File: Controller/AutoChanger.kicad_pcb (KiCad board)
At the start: 2 copper layers, 118 x 74.1 mm, 32 parts, among them J1 OLED, P10 SENSOR, P11 SENSOR, P12 LOGO, P3 1, P4 2, P5 3, P6 4, P8 M3, P9 M3, SW1 RESET, SW2 1, SW3 2, SW4 3, SW5 4, SW6 PRGM, U1 TinyPico, U2 PCA9685PW, U3 ITR9606-F

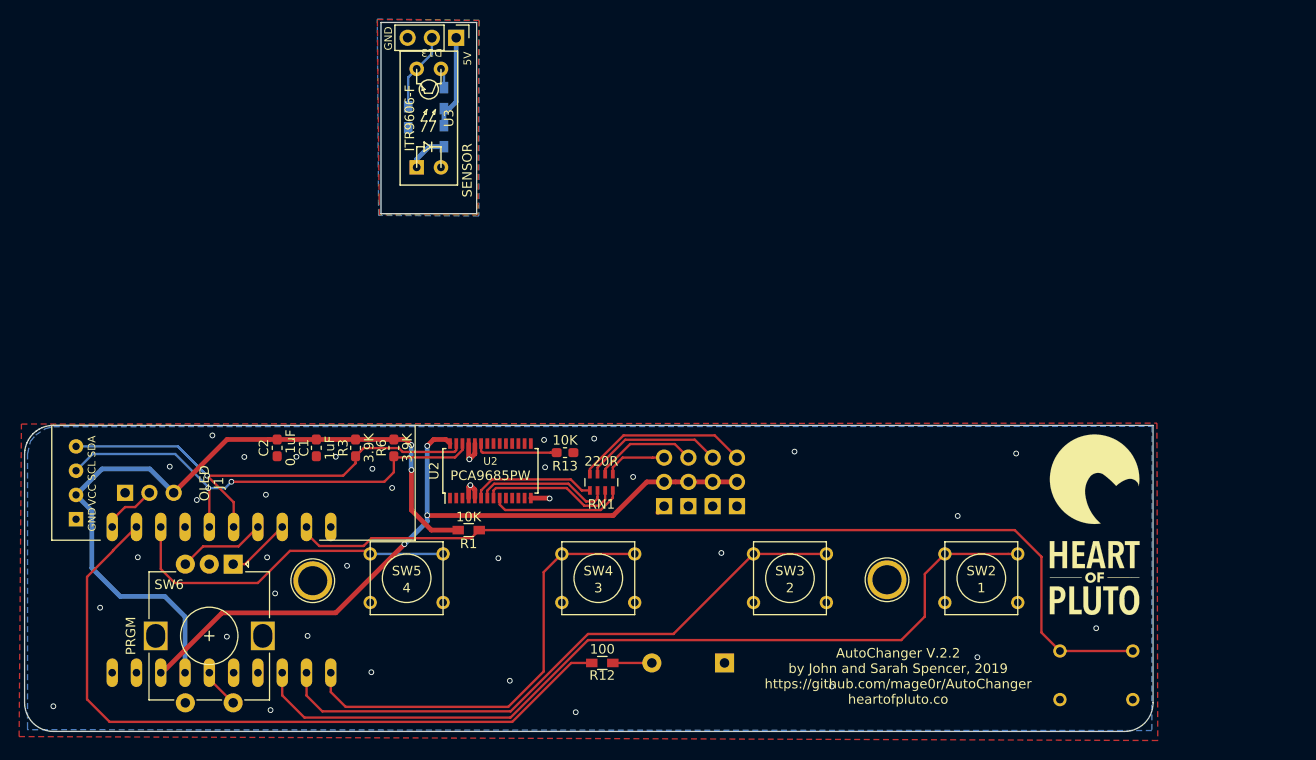
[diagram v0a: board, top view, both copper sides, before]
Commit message: Circuit Board updated to version 3.0
Circuit board no longer uses a TinyPICO.  It uses a ESP32-S3-WROOM module instead.  It is also 90% SMD parts and can be assembled by JLCPCB
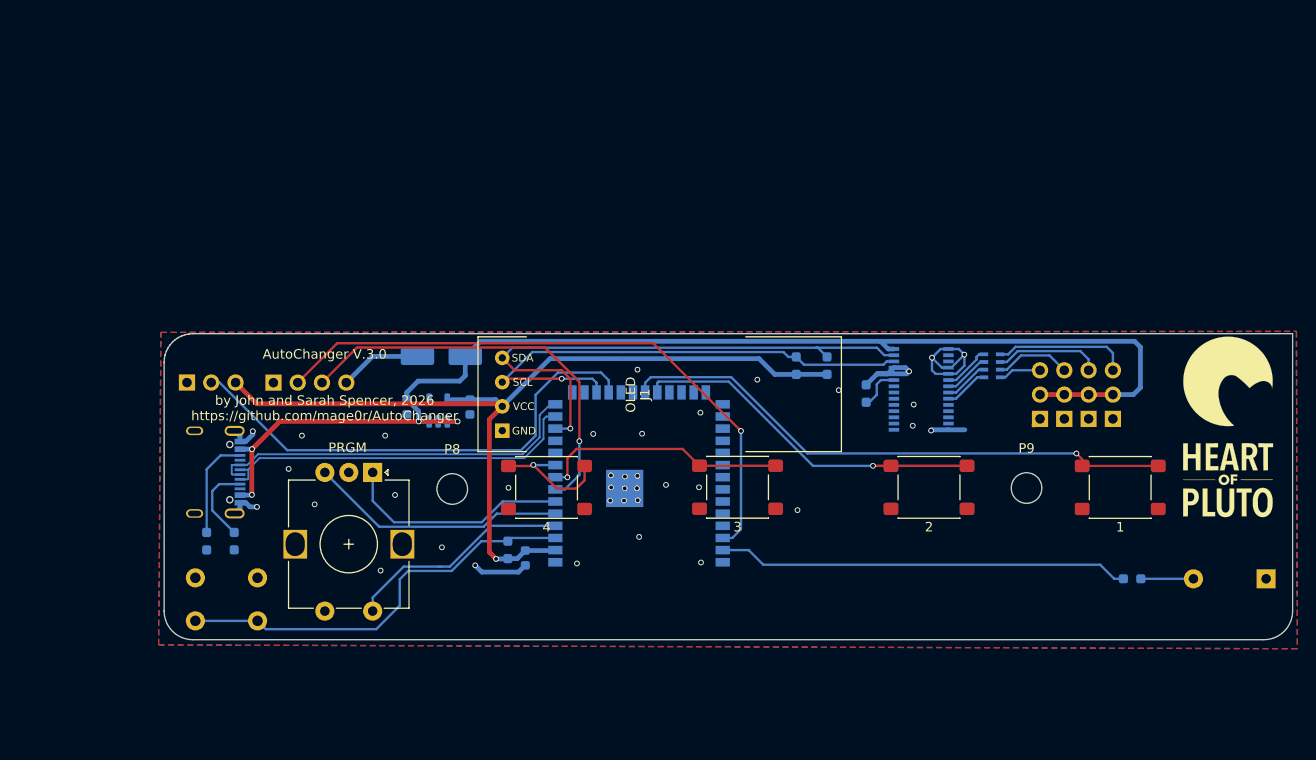
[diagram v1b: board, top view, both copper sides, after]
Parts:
- removed C1: 1uF, Capacitor_SMD:C_0603_1608Metric_Pad1.05x0.95mm_HandSolder
- removed C2: 0.1uF, Capacitor_SMD:C_0603_1608Metric_Pad1.05x0.95mm_HandSolder
- removed P11: SENSOR, Pin_Headers:Pin_Header_Straight_1x03_Pitch2.54mm
- removed R2, R4: 220R, Resistors_SMD:R_0603_HandSoldering
- removed R3, R6: 3.9K, Resistor_SMD:R_0603_1608Metric_Pad1.05x0.95mm_HandSolder
- removed R5: 2M, Resistors_SMD:R_0603_HandSoldering
- removed U1: TinyPico, libs:TinyPico
- removed U3: ITR9606-F, libs:ITR9606
- added C3: 22uF, Capacitor_SMD:C_0603_1608Metric, B.Cu at (141.6, 93.9)
- added C8: 10uF, Capacitor_SMD:C_0603_1608Metric, B.Cu at (129.2, 78.1)
- added C9: 10uF, Capacitor_SMD:C_0603_1608Metric, B.Cu at (135.8, 78.1)
- added D1: SS14, Diode_SMD:D_SMA_Handsoldering, B.Cu at (132.8, 72.8)
- added J2: USB-C, libs:AMPHENOL_12402012E212A, B.Cu at (107.0, 84.9)
- added J3: I2C, Connector_PinHeader_2.54mm:PinHeader_1x04_P2.54mm_Vertical, B.Cu at (115.2, 75.6)
- added R15: 5.1k, Resistor_SMD:R_0603_1608Metric_Pad0.98x0.95mm_HandSolder, B.Cu at (108.2, 92.2)
- added R16: 5.1k, Resistor_SMD:R_0603_1608Metric_Pad0.98x0.95mm_HandSolder, B.Cu at (111.1, 92.2)
- added R17: 4.7K, Resistor_SMD:R_0603_1608Metric_Pad0.98x0.95mm_HandSolder, B.Cu at (173.1, 73.8)
- added R18: 4.7K, Resistor_SMD:R_0603_1608Metric_Pad0.98x0.95mm_HandSolder, B.Cu at (169.9, 73.8)
- added U4: AP2112K-3.3, Package_TO_SOT_SMD:SOT-23-5, B.Cu at (132.4, 78.5)
- added U5: ESP32-S3-WROOM-1, RF_Module:ESP32-S3-WROOM-1, B.Cu at (153.4, 89.1)
- P10, P3, P4, P5, P6: footprint Pin_Headers:Pin_Header_Straight_1x03_Pitch2.54mm -> Connector_PinHeader_2.54mm:PinHeader_1x03_P2.54mm_Vertical
- P8, P9: footprint Connect:1pin -> MountingHole:MountingHole_3.2mm_M3
- R1: footprint Resistors_SMD:R_0603_HandSoldering -> Resistor_SMD:R_0603_1608Metric_Pad0.98x0.95mm_HandSolder; moved to B.Cu
- R12: value 100 -> 100R; footprint Resistors_SMD:R_0603_HandSoldering -> Resistor_SMD:R_0603_1608Metric_Pad0.98x0.95mm_HandSolder; moved to B.Cu
- R13: footprint Resistor_SMD:R_0603_1608Metric_Pad1.05x0.95mm_HandSolder -> Resistor_SMD:R_0603_1608Metric_Pad0.98x0.95mm_HandSolder; moved to B.Cu
- RN1, U2: moved to B.Cu
- SP1: footprint Buzzers_Beepers:Buzzer_12x9.5RM7.6 -> Buzzer_Beeper:Buzzer_12x9.5RM7.6
- SW1: footprint Buttons_Switches_ThroughHole:SW_PUSH_SMALL -> Button_Switch_THT:SW_PUSH_6mm
- SW2, SW3, SW4, SW5: footprint Buttons_Switches_ThroughHole:SW_PUSH_SMALL -> Button_Switch_SMD:SW_SPST_PTS645Sx43SMTR92
- moved SW1 94.4 mm to (107.0, 100.5), turned to 0 degrees
- moved SP1 57.3 mm to (219.0, 96.1)
- moved R12 56.1 mm to (205.0, 96.1)
- moved U2 45.8 mm to (182.9, 76.3), turned to 180 degrees
- moved J1 45.5 mm to (155.6, 76.8)
- moved RN1 42.6 mm to (190.3, 73.8), turned to 0 degrees
- moved P3 40.4 mm to (203.0, 79.4)
- moved P4 40.4 mm to (200.4, 79.4)
- moved P5 40.4 mm to (197.9, 79.4)
- moved P6 40.4 mm to (195.4, 79.4)
- moved R13 32.1 mm to (177.2, 76.7), turned to 90 degrees
- moved P8 17.5 mm to (133.9, 86.7)
- moved P9 17.5 mm to (194.0, 86.6)
- moved SW6 17.5 mm to (125.6, 85.0)
- moved SW5 17.4 mm to (143.8, 86.5)
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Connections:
- net +3V3 renamed +3.3V
- net /RESET renamed /EN
- P10 pad 2: /GPIO23 -> /IO10
- R12 pad 1: /GPIO19 -> /IO1
- RN1 pad 1: Net-(RN1-Pad1) -> Net-(RN1-R1.1)
- RN1 pad 2: Net-(RN1-Pad2) -> Net-(RN1-R2.1)
- RN1 pad 3: Net-(RN1-Pad3) -> Net-(RN1-R3.1)
- RN1 pad 4: Net-(RN1-Pad4) -> Net-(RN1-R4.1)
- RN1 pad 5: /PWM3 -> /PWM0
- RN1 pad 6: /PWM2 -> /PWM1
- RN1 pad 7: /PWM1 -> /PWM2
- RN1 pad 8: /PWM0 -> /PWM3
- SW2 pad 1: /GPIO27 -> /BTN_1
- SW3 pad 1: /GPIO26 -> /BTN_2
- SW4 pad 1: /GPIO25 -> /BTN_3
- SW5 pad 1: /GPIO18 -> /BTN_4
- SW6 pad A: /GPIO33 -> /IO6
- SW6 pad B: /GPIO32 -> /IO5
- SW6 pad S1: /GPIO4 -> /IO4
- U2 pad 10: Net-(U2-Pad10) -> unconnected-(U2-LED4-Pad10)
- U2 pad 11: Net-(U2-Pad11) -> unconnected-(U2-LED5-Pad11)
- U2 pad 12: Net-(U2-Pad12) -> unconnected-(U2-LED6-Pad12)
- U2 pad 13: Net-(U2-Pad13) -> unconnected-(U2-LED7-Pad13)
- U2 pad 15: Net-(U2-Pad15) -> unconnected-(U2-LED8-Pad15)
- U2 pad 16: Net-(U2-Pad16) -> unconnected-(U2-LED9-Pad16)
- U2 pad 17: Net-(U2-Pad17) -> unconnected-(U2-LED10-Pad17)
- U2 pad 18: Net-(U2-Pad18) -> unconnected-(U2-LED11-Pad18)
- U2 pad 19: Net-(U2-Pad19) -> unconnected-(U2-LED12-Pad19)
- U2 pad 20: Net-(U2-Pad20) -> unconnected-(U2-LED13-Pad20)
- U2 pad 21: Net-(U2-Pad21) -> unconnected-(U2-LED14-Pad21)
- U2 pad 22: Net-(U2-Pad22) -> unconnected-(U2-LED15-Pad22)
- U2 pad 6: Net-(RN1-Pad1) -> Net-(RN1-R4.1)
- U2 pad 7: Net-(RN1-Pad2) -> Net-(RN1-R3.1)
- U2 pad 8: Net-(RN1-Pad3) -> Net-(RN1-R2.1)
- U2 pad 9: Net-(RN1-Pad4) -> Net-(RN1-R1.1)
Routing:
- net /GPIO27: track 89.9 -> 0.00 mm
- net /GPIO19: track 76.5 -> 0.00 mm
- net /IO2: track 0.00 -> 64.4 mm, vias 0 -> 1
- net /GPIO26: track 64.3 -> 0.00 mm
- net /BTN_1: track 0.00 -> 59.2 mm, vias 0 -> 1
- net /EN: track 98.2 -> 43.6 mm
- net +5V: track 79.4 -> 133.2 mm, vias 3 -> 4
- net /IO10: track 0.00 -> 51.9 mm
- net /GPIO25: track 47.6 -> 0.00 mm
- net /IO1: track 0.00 -> 43.1 mm
- net /IO7: track 0.00 -> 42.8 mm, vias 0 -> 1
- net /D+: track 0.00 -> 39.6 mm
- net /D-: track 0.00 -> 38.3 mm
- net /BTN_2: track 0.00 -> 37.1 mm, vias 0 -> 1
- net /GPIO18: track 36.1 -> 0.00 mm
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- removed copper zone on B.Cu, net /GND_C
- removed copper zone on F.Cu, net /GND_C
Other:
- board size 118 x 74.1 mm -> 118 x 32 mm
- board text added: "AutoChanger V.3.0 by John and Sarah Spencer, 2026 https://github.com/mage0r/AutoChanger"
- board text added: "IO10"
- board text removed: "AutoChanger V.2.2 by John and Sarah Spencer, 2019 https://github.com/mage0r/AutoChanger heartofpluto.co"
- board text removed: "D13"
- board text removed: "D23"
- board text removed: "SENSOR"

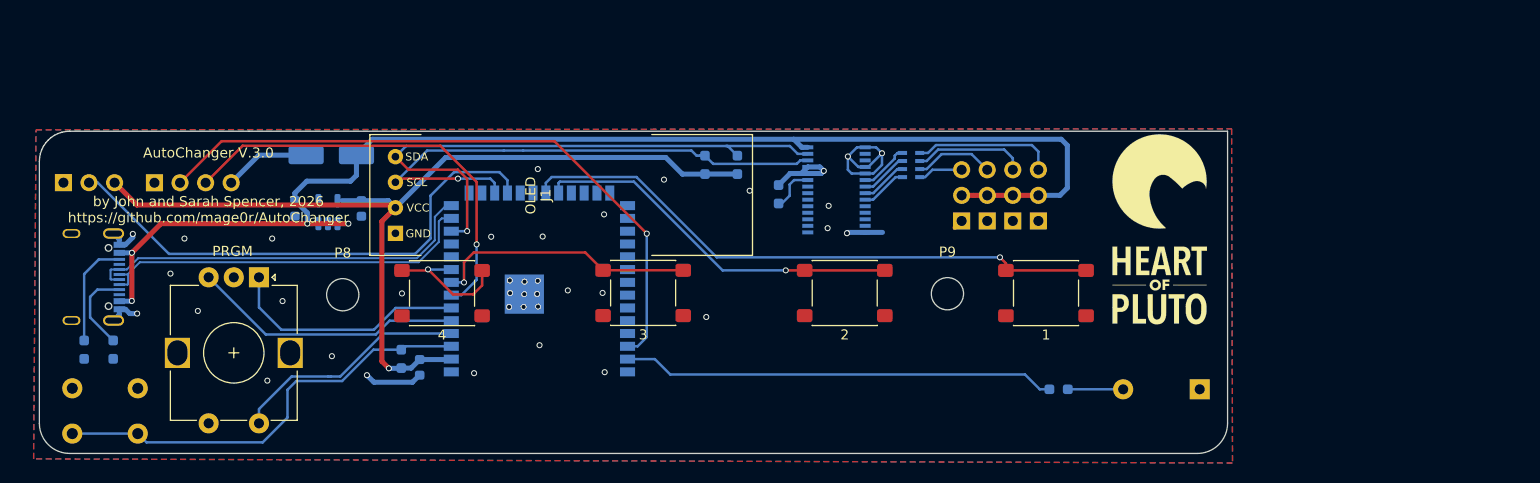
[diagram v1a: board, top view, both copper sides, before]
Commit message: changes to jlcpcb tags
Improving jlcpcb manufacturability.  Ideally none of the parts are hand placed.
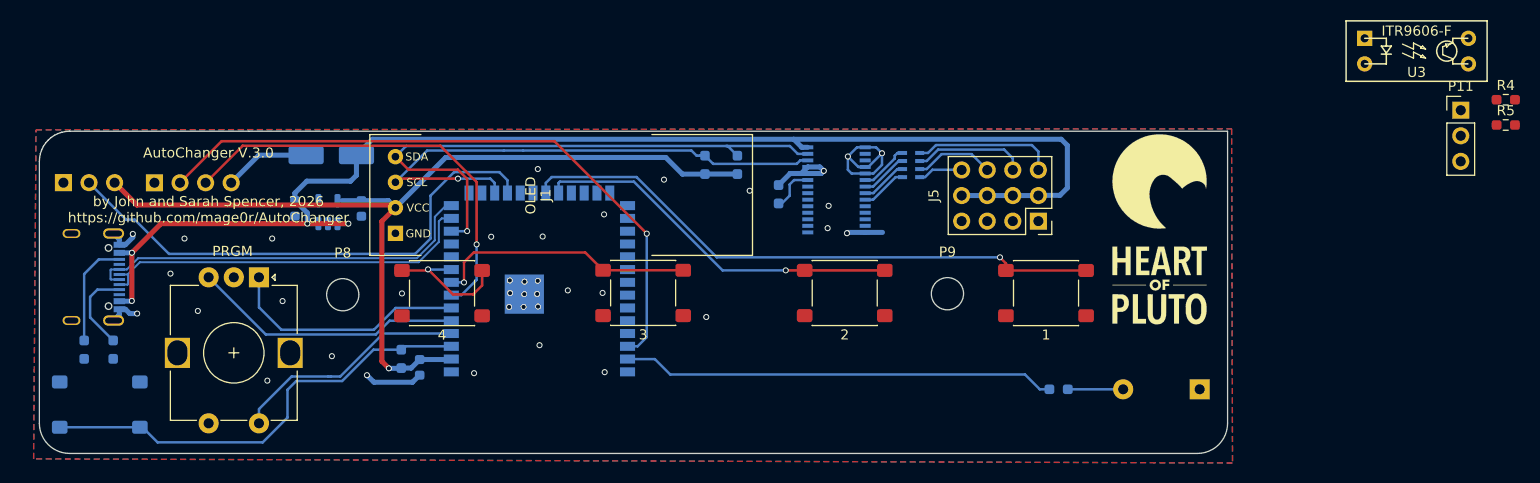
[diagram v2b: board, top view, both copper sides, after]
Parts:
- removed P3: 1, Connector_PinHeader_2.54mm:PinHeader_1x03_P2.54mm_Vertical
- removed P4: 2, Connector_PinHeader_2.54mm:PinHeader_1x03_P2.54mm_Vertical
- removed P5: 3, Connector_PinHeader_2.54mm:PinHeader_1x03_P2.54mm_Vertical
- removed P6: 4, Connector_PinHeader_2.54mm:PinHeader_1x03_P2.54mm_Vertical
- added J5: HX PZ2.54-4x3P, libs:HX PZ2.54-4x3P, F.Cu at (203.0, 79.4)
- added P11: SENSOR, Connector_PinHeader_2.54mm:PinHeader_1x03_P2.54mm_Vertical, F.Cu at (244.9, 68.4)
- added R4: 100R, Resistor_SMD:R_0603_1608Metric_Pad0.98x0.95mm_HandSolder, F.Cu at (249.4, 67.3)
- added R5: 10K, Resistor_SMD:R_0603_1608Metric_Pad0.98x0.95mm_HandSolder, F.Cu at (249.4, 69.8)
- added U3: ITR9606-F, libs:ITR9606, F.Cu at (240.5, 62.5)
- SW1: footprint Button_Switch_THT:SW_PUSH_6mm -> Button_Switch_SMD:SW_SPST_PTS645Sx43SMTR92
- moved SW1 3.97 mm to (109.8, 97.6)
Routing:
- net /EN: track 43.6 -> 45.1 mm
- net GND: track 40.6 -> 39.6 mm
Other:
- board text removed: "5V"

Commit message: Circuit board Version 3.1
Improvements made to allow manufacturing with PnP machines.
Geometry is largely unchanged.
i2c for connections to other systems now has level shifting.
the sensor and the i2c connector are now using PST 2.0 plugs rather than dupont.
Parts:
- removed J5: HX PZ2.54-4x3P, libs:HX PZ2.54-4x3P
- added J4: 03-04, libs:HDR-SMD_6P-P2.54-V-M-R2-C3-LS7.5-2, B.Cu at (121.4, 144.1)
- added J6: 01-02, libs:HDR-SMD_6P-P2.54-V-M-R2-C3-LS7.5-2, B.Cu at (130.5, 144.1)
- added Q1: BSS138, Package_TO_SOT_SMD:SOT-23, B.Cu at (92.7, 159.9)
- added Q2: BSS138, Package_TO_SOT_SMD:SOT-23, B.Cu at (92.7, 148.7)
- added RN2: 10K, Resistor_SMD:R_Array_Convex_4x0603, B.Cu at (92.6, 154.4)
- D1: footprint Diode_SMD:D_SMA_Handsoldering -> Diode_SMD:D_SMA
- J3: footprint Connector_PinHeader_2.54mm:PinHeader_1x04_P2.54mm_Vertical -> libs:CONN-SMD_PH2.0MM-4P-WT
- P10: footprint Connector_PinHeader_2.54mm:PinHeader_1x03_P2.54mm_Vertical -> libs:CONN-SMD_PH2.0MM-3P-WT
- U3: moved to B.Cu
- moved R4 209.1 mm to (41.3, 46.8), turned to 180 degrees
- moved R5 209.0 mm to (41.3, 50.6)
- moved P11 201.0 mm to (44.1, 58.6), turned to -90 degrees
- moved U3 199.6 mm to (41.4, 48.8), turned to -90 degrees
- moved R12 125.8 mm to (98.0, 162.3)
- moved P12 119.5 mm to (125.6, 159.6)
- moved J2 104.5 mm to (29.4, 154.9)
- moved R15 103.9 mm to (30.4, 160.9), turned to 180 degrees
- moved R16 103.4 mm to (33.9, 160.9), turned to 0 degrees
- moved C3 103.0 mm to (64.0, 161.6)
- moved D1 103.0 mm to (55.2, 140.6)
- moved P9 103.0 mm to (116.4, 154.3)
- moved C8 103.0 mm to (51.6, 145.8)
- moved C9 103.0 mm to (58.2, 145.8)
- moved J1 103.0 mm to (78.0, 144.5)
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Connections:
- J3 pad 2: /IO2 -> /SDA_B_5V
- J3 pad 3: /IO7 -> /SCL_B_5v
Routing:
- net /SDA_B_5V: track 0.00 -> 75.9 mm, vias 0 -> 2
- net /SCL_B_5v: track 0.00 -> 64.6 mm, vias 0 -> 2
- net /IO2: track 64.4 -> 15.1 mm, vias 1 -> 0
- net +5V: track 132.8 -> 168.7 mm, vias 4 -> 6
- net Net-(R12-Pad2): track 5.50 -> 35.5 mm
- net /IO1: track 43.1 -> 13.1 mm
- net +3.3V: track 95.0 -> 119.2 mm, vias 1 -> 4
- net /3V3_C: track 0.00 -> 13.4 mm
- net /IO7: track 42.8 -> 30.2 mm, vias 1 -> 2
- net /GPIO23_C: track 0.00 -> 8.58 mm
- net /PWM0: track 14.2 -> 20.7 mm
- net /PWM1: track 11.2 -> 15.3 mm
- net /PWM2: track 7.97 -> 11.5 mm
- net Net-(R4-Pad2): track 0.00 -> 3.25 mm
- net /IO10: track 51.9 -> 49.7 mm
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- added copper zone on B.Cu, net /GND_C
- added copper zone on F.Cu, net /GND_C
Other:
- board size 118 x 32 mm -> 118 x 129.7 mm
- board text added: "+5V"
- board text added: "AutoChanger V.3.1 by John and Sarah Spencer, 2026 https://github.com/mage0r/AutoChanger"
- board text added: "IO2"
- board text added: "IO7"
